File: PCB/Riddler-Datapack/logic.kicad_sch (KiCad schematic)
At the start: 7 parts, among them SW1 RST, SW2 BOOT, U13 ESP32-S3-WROOM-1U-N16R8

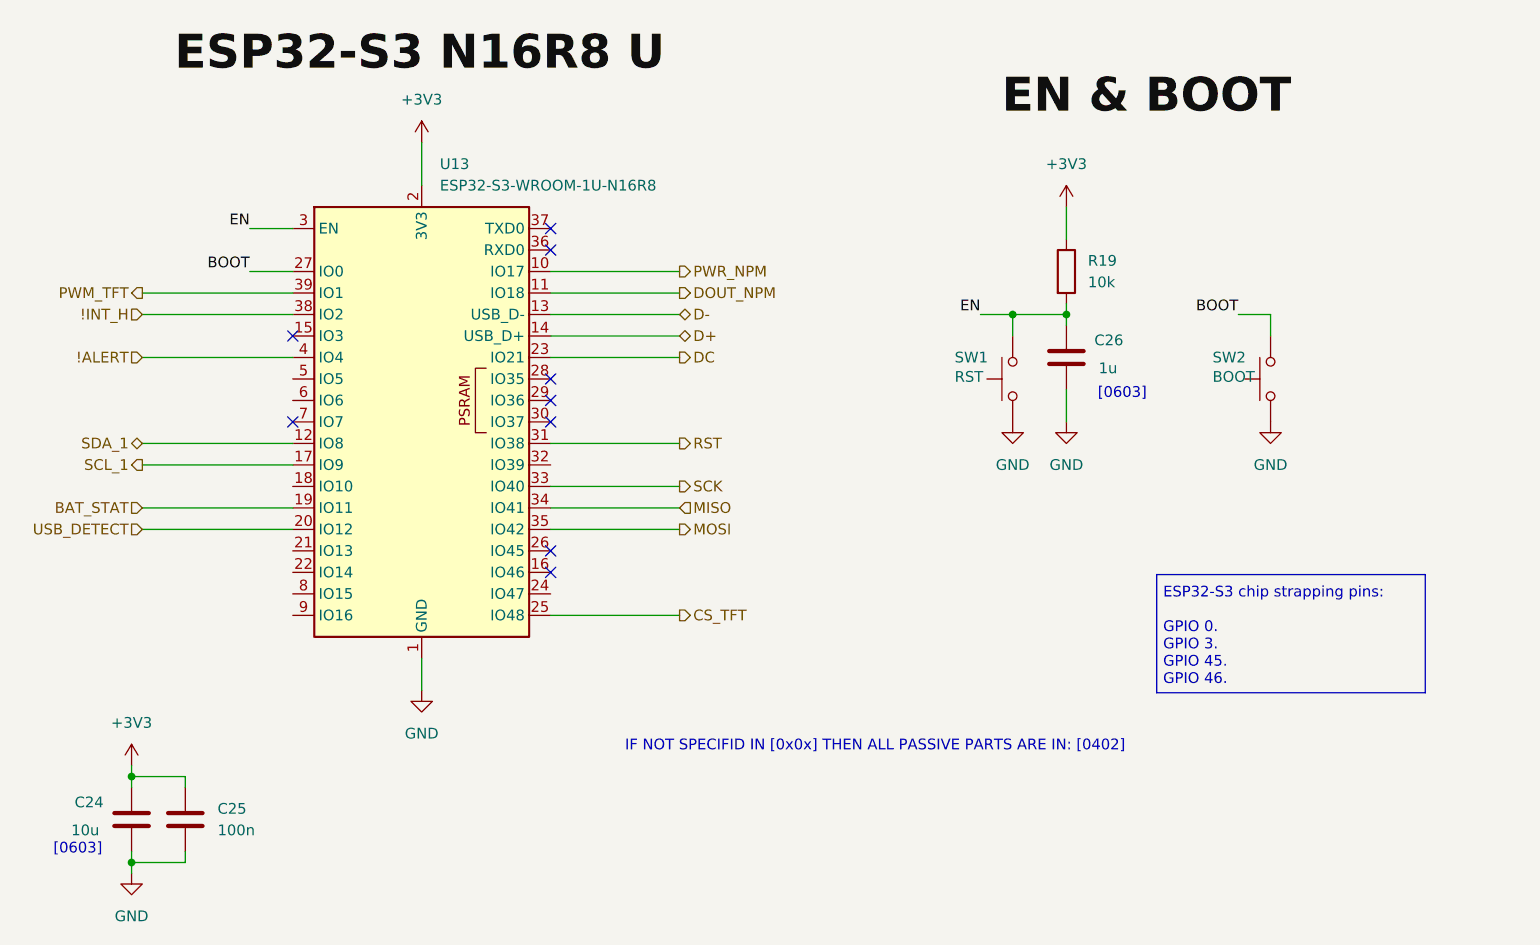
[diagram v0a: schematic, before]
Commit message: Complete schematics v0.5, add schematic PDF export and active prop reference
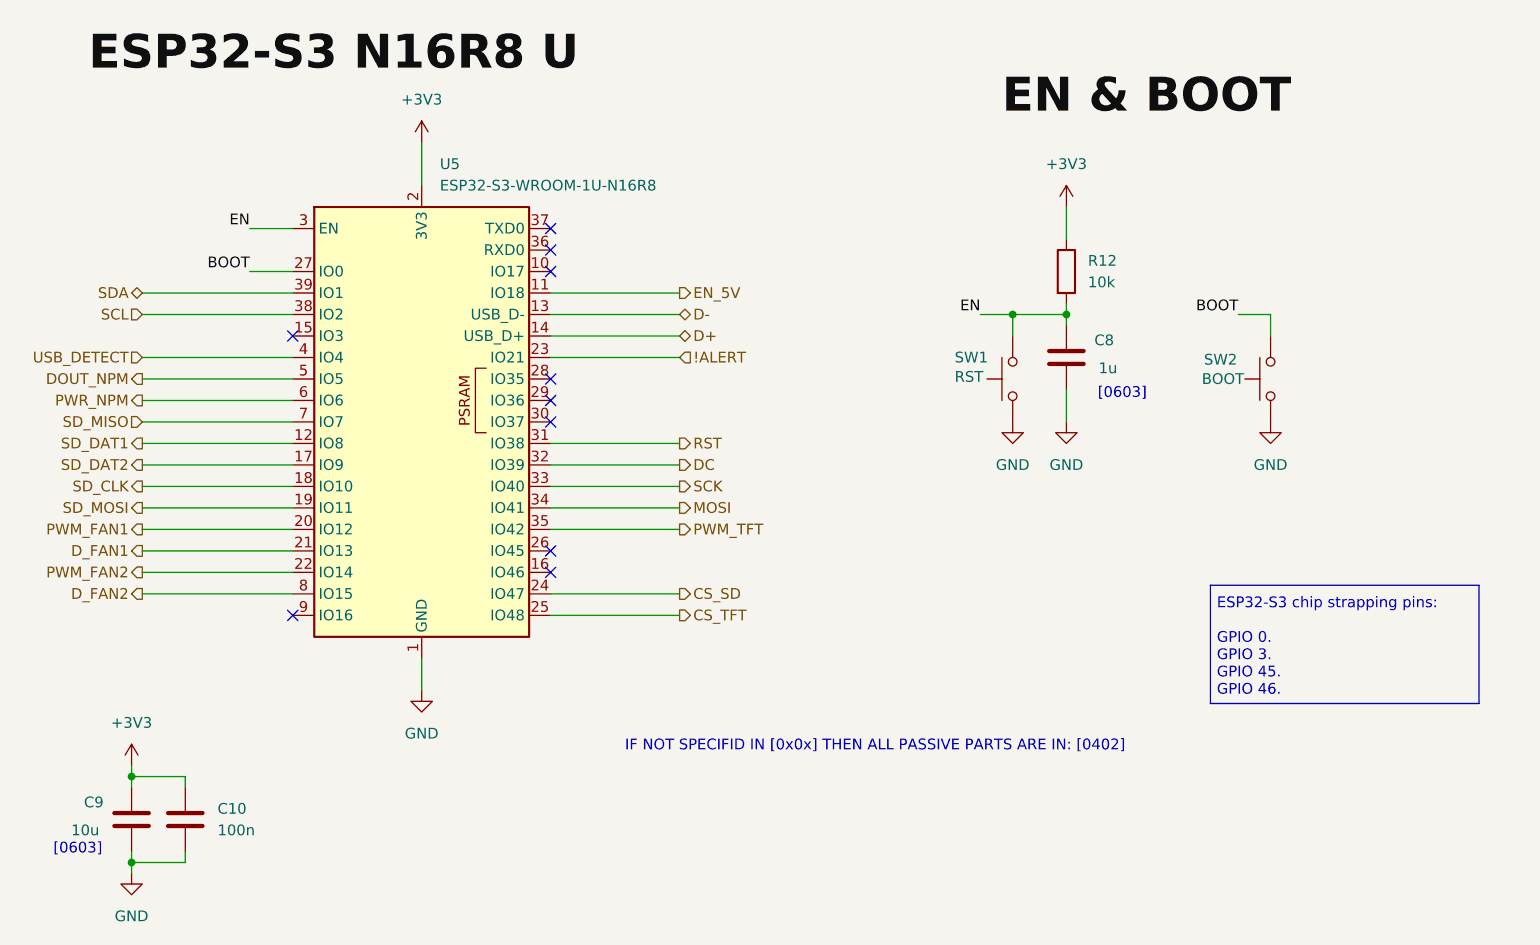
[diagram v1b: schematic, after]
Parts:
- renumbered C25 to C10, C26 to C8, C24 to C9, R19 to R12, U13 to U5
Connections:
- net MISO is gone; now on net MOSI: U5.34 (IO41)
- net !ALERT: now also U5.23 (IO21); no longer U5.4 (IO4)
- net DC: now also U5.32 (IO39); no longer U5.23 (IO21)
- net DOUT_NPM: now also U5.5 (IO5); no longer U5.11 (IO18)
- net MOSI: no longer U5.35 (IO42)
- net PWM_TFT: now also U5.35 (IO42); no longer U5.39 (IO1)
- net PWR_NPM: now also U5.6 (IO6); no longer U5.10 (IO17)
- net USB_DETECT: now also U5.4 (IO4); no longer U5.20 (IO12)
- net SD_CLK: now reaches U5.18 (IO10)
- net D_FAN1: now reaches U5.21 (IO13)
- net PWM_FAN2: now reaches U5.22 (IO14)
- net CS_SD: now reaches U5.24 (IO47)
- net SD_MISO: now reaches U5.7 (IO7)
- net D_FAN2: now reaches U5.8 (IO15)
- net !INT_H renamed SCL
- net BAT_STAT renamed SD_MOSI
- net SCL_1 renamed SD_DAT2
- net SDA_1 renamed SD_DAT1
- new net EN_5V: U5.11 (IO18)
- new net PWM_FAN1: U5.20 (IO12)
- new net SDA: U5.39 (IO1)
- no-connect marks 9 -> 10
